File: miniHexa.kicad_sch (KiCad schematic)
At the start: 16 parts, among them U1 STM32F401RETx, Y1 16Mhz

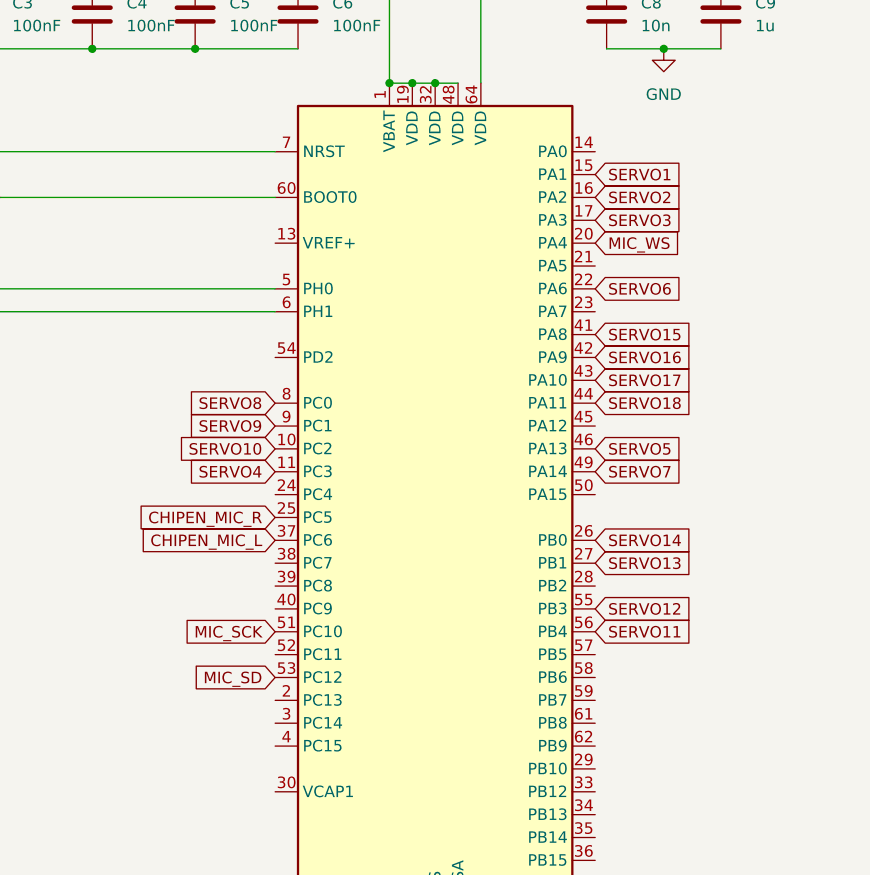
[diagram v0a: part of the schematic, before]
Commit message: added 16 channel servo PWM controller
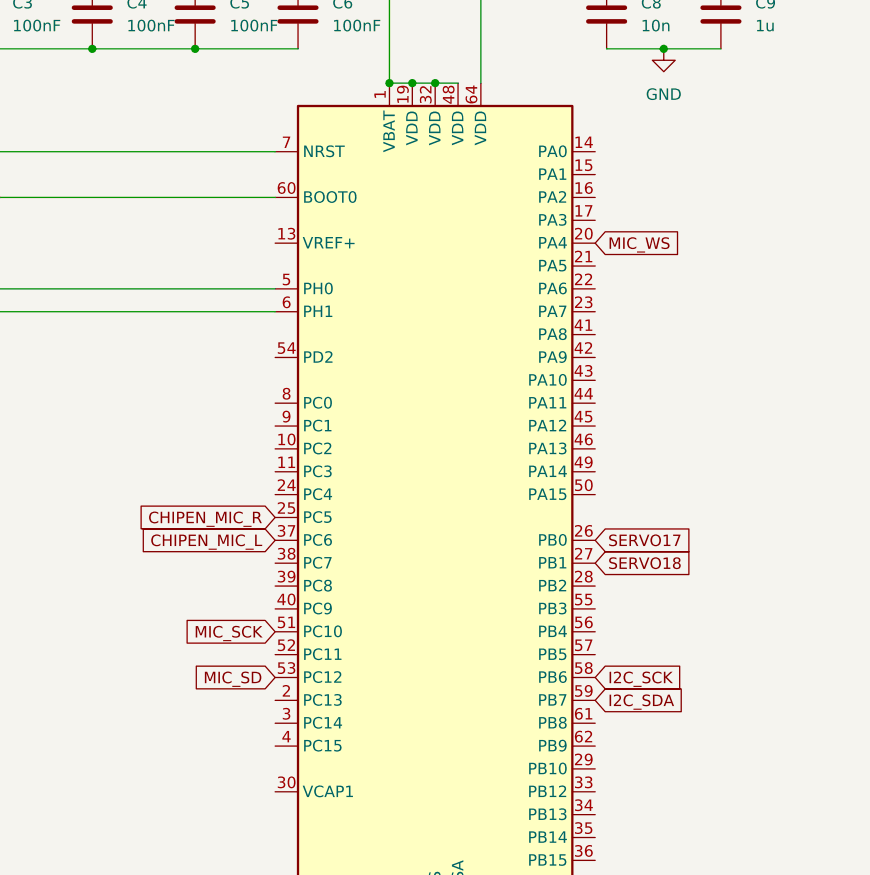
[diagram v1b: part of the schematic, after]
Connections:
- net SERVO13 is gone; now on net SERVO18: U1.27 (PB1)
- net SERVO14 is gone; now on net SERVO17: U1.26 (PB0)
- net SERVO17: no longer U1.43 (PA10)
- net SERVO18: no longer U1.44 (PA11)
- net I2C_SCK: now reaches U1.58 (PB6)
- net I2C_SDA: now reaches U1.59 (PB7)
- net SERVO1: no longer names the net of U1.15 (PA1)
- net SERVO10: no longer names the net of U1.10 (PC2)
- net SERVO11: no longer names the net of U1.56 (PB4)
- net SERVO12: no longer names the net of U1.55 (PB3)
- net SERVO15: no longer names the net of U1.41 (PA8)
- net SERVO16: no longer names the net of U1.42 (PA9)
- net SERVO2: no longer names the net of U1.16 (PA2)
- net SERVO3: no longer names the net of U1.17 (PA3)
- net SERVO4: no longer names the net of U1.11 (PC3)
- net SERVO5: no longer names the net of U1.46 (PA13)
- net SERVO6: no longer names the net of U1.22 (PA6)
- net SERVO7: no longer names the net of U1.49 (PA14)
- net SERVO8: no longer names the net of U1.8 (PC0)
- net SERVO9: no longer names the net of U1.9 (PC1)

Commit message: assigned footprints and I2c for stm32
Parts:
- MK1, MK2: footprint Microphone:MIC_INMP441ACEZ-R7 -> Audio_Module:MIC_INMP441ACEZ-R7
- R29: footprint (none) -> Resistor_SMD:R_0805_2012Metric
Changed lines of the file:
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@@
 			)
 		)
-		(property "Footprint" "Microphone:MIC_INMP441ACEZ-R7"
+		(property "Footprint" "Audio_Module:MIC_INMP441ACEZ-R7"
 			(at 48.26 172.72 0)
 			(effects
@@
 			)
 		)
-		(property "Footprint" ""
+		(property "Footprint" "Resistor_SMD:R_0805_2012Metric"
 			(at 93.472 179.07 90)
 			(effects
@@
 			)
 		)
-		(property "Footprint" "Microphone:MIC_INMP441ACEZ-R7"
+		(property "Footprint" "Audio_Module:MIC_INMP441ACEZ-R7"
 			(at 118.11 172.72 0)
 			(effects

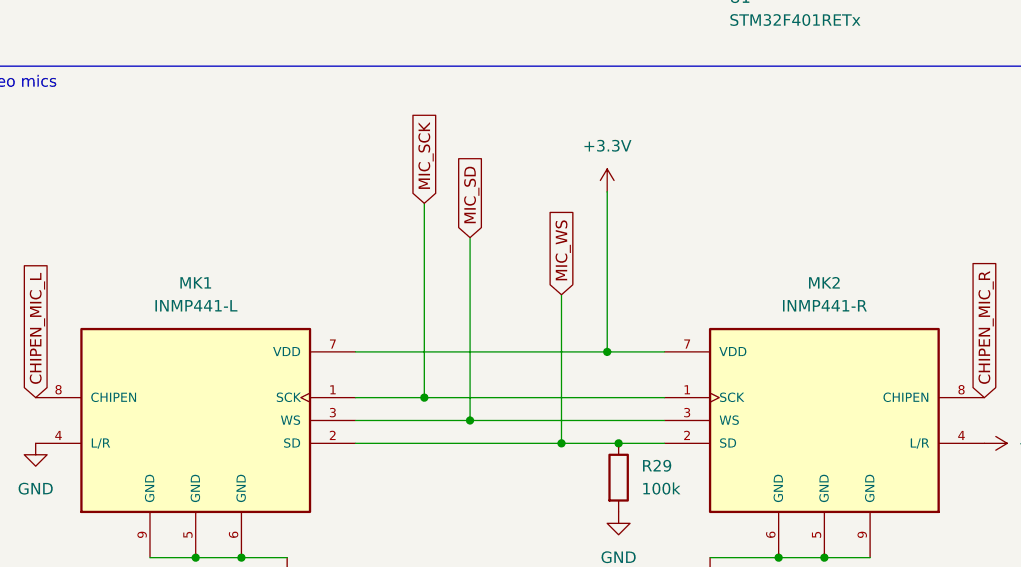
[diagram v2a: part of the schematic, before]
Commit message: Removed redundent components
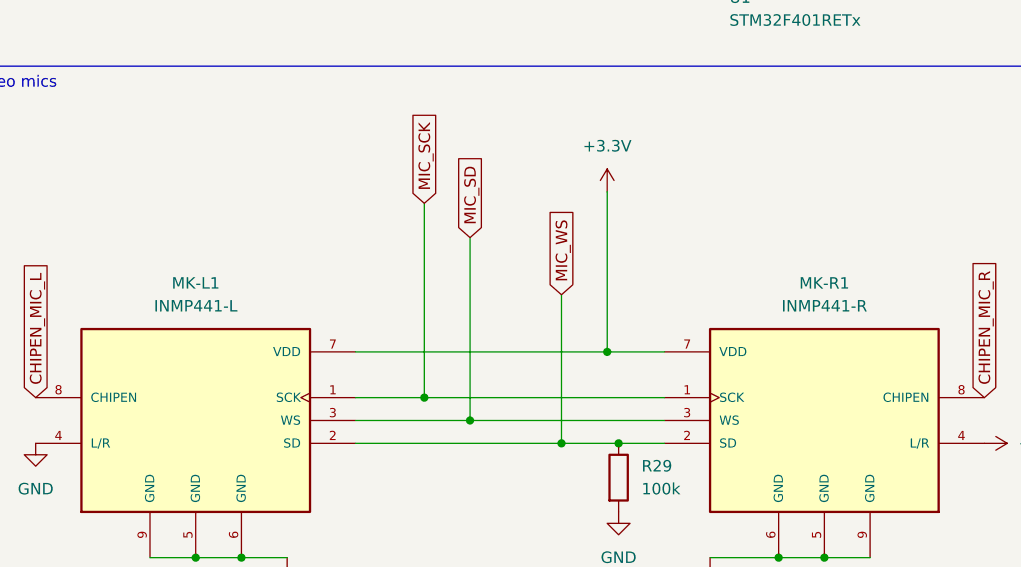
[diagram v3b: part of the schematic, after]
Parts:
- renumbered MK1 to MK-L1, MK2 to MK-R1
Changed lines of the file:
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@@
 		(dnp no)
 		(fields_autoplaced yes)
-		(property "Reference" "MK1"
+		(property "Reference" "MK-L1"
 			(at 48.26 157.48 0)
 			(effects
@@
 			(project "miniHexa"
 				(path "/3449ee66-2977-4802-a474-0821cdf4e79b"
-					(reference "MK1")
+					(reference "MK-L1")
 					(unit 1)
 				)
@@
 		(on_board yes)
 		(dnp no)
-		(property "Reference" "MK2"
+		(property "Reference" "MK-R1"
 			(at 118.11 157.48 0)
 			(effects
@@
 			(project "miniHexa"
 				(path "/3449ee66-2977-4802-a474-0821cdf4e79b"
-					(reference "MK2")
-					(unit 1)
-				)
+					(reference "MK-R1")
+					(unit 1)
+				)
